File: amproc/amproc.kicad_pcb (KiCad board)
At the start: 2 copper layers, 150 x 70 mm, 130 parts, among them J1 OUT, J2 AC IN, J3 METER BRIDGE, J4 STEREO LINK, J5 LEFT IN, J6 RIGHT IN, J7 CHASSIS, J8 EXT POWER, J9 EXT POWER, Q1 BC556, Q2 BC546, Q3 BC546, Q4 BC556, Q5 BC546, Q6 BC556, Q7 BC556, Q8 BC556, Q9 BC556, U1 TL072, U2 TL072, U3 TL072, U4 LM13700, U5 TL072, U6 TL072, U7 TL072, U8 L7815, U9 L7915

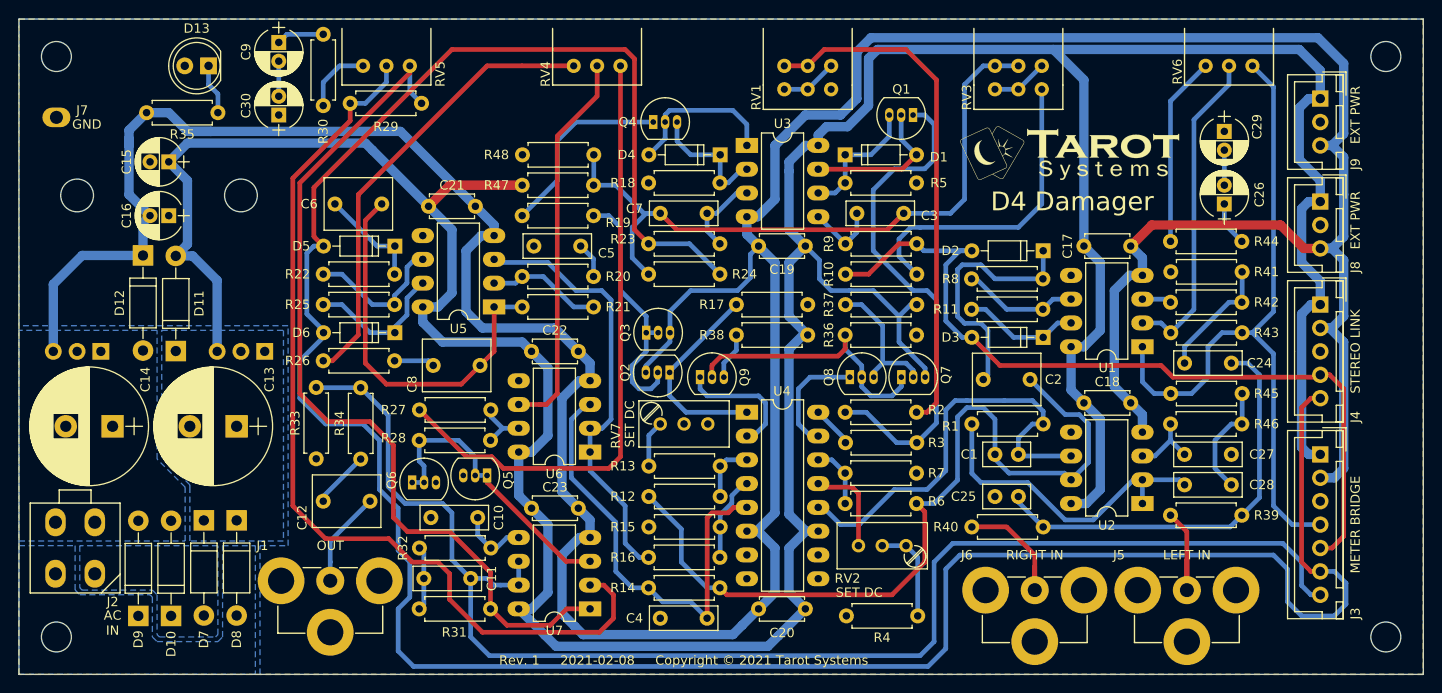
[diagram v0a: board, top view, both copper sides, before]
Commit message: Upgrade amproc to Kicad 6
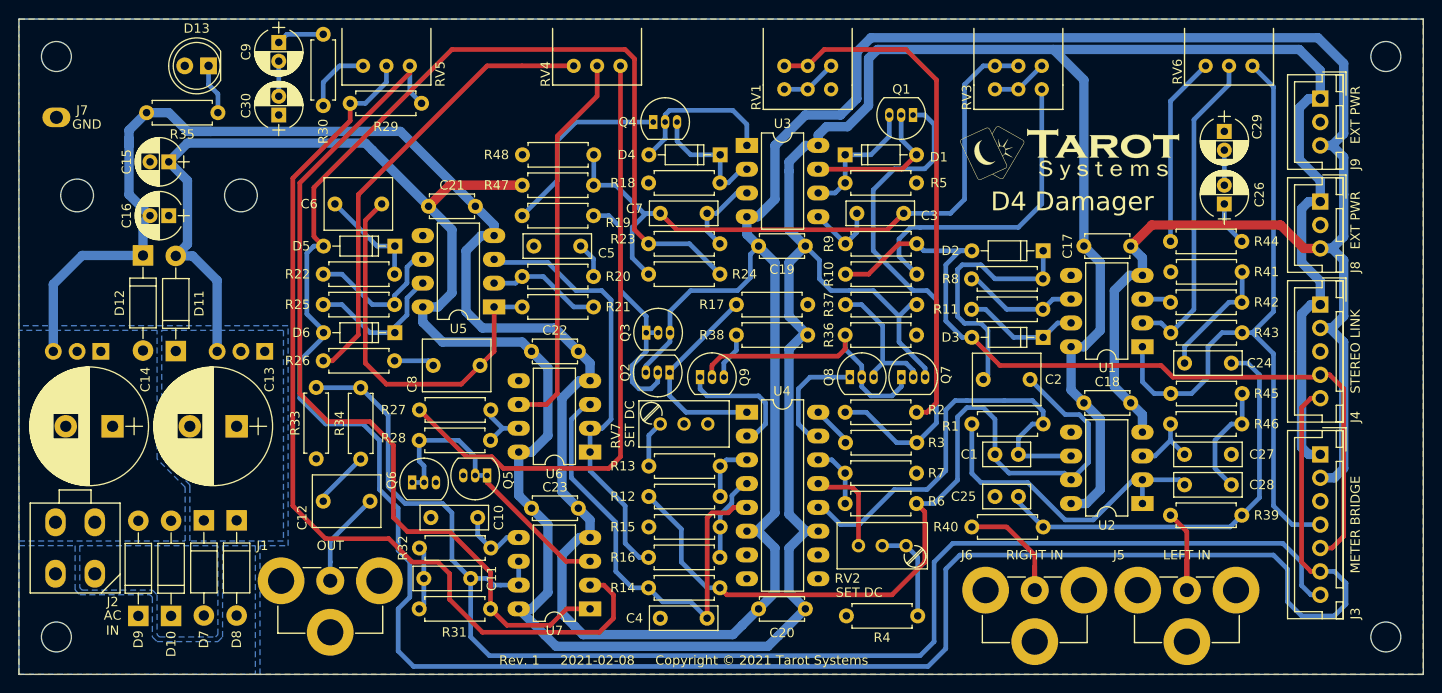
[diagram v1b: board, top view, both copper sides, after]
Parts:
- C25: value 560p -> 100p
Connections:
- net /Limiter.sch/IN renamed /Input stage/OUT
- net /Preemphasis/IN renamed /Limiter.sch/OUT
- U4 pad 10: Net-(U4-Pad10) -> unconnected-(U4-Pad10)
- U4 pad 7: Net-(U4-Pad7) -> unconnected-(U4-Pad7)
- U4 pad 8: Net-(U4-Pad8) -> unconnected-(U4-Pad8)
- U4 pad 9: Net-(U4-Pad9) -> unconnected-(U4-Pad9)
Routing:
- net Net-(C27-Pad2): track 8.39 -> 7.56 mm
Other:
- net class Default removed
- net class Power removed

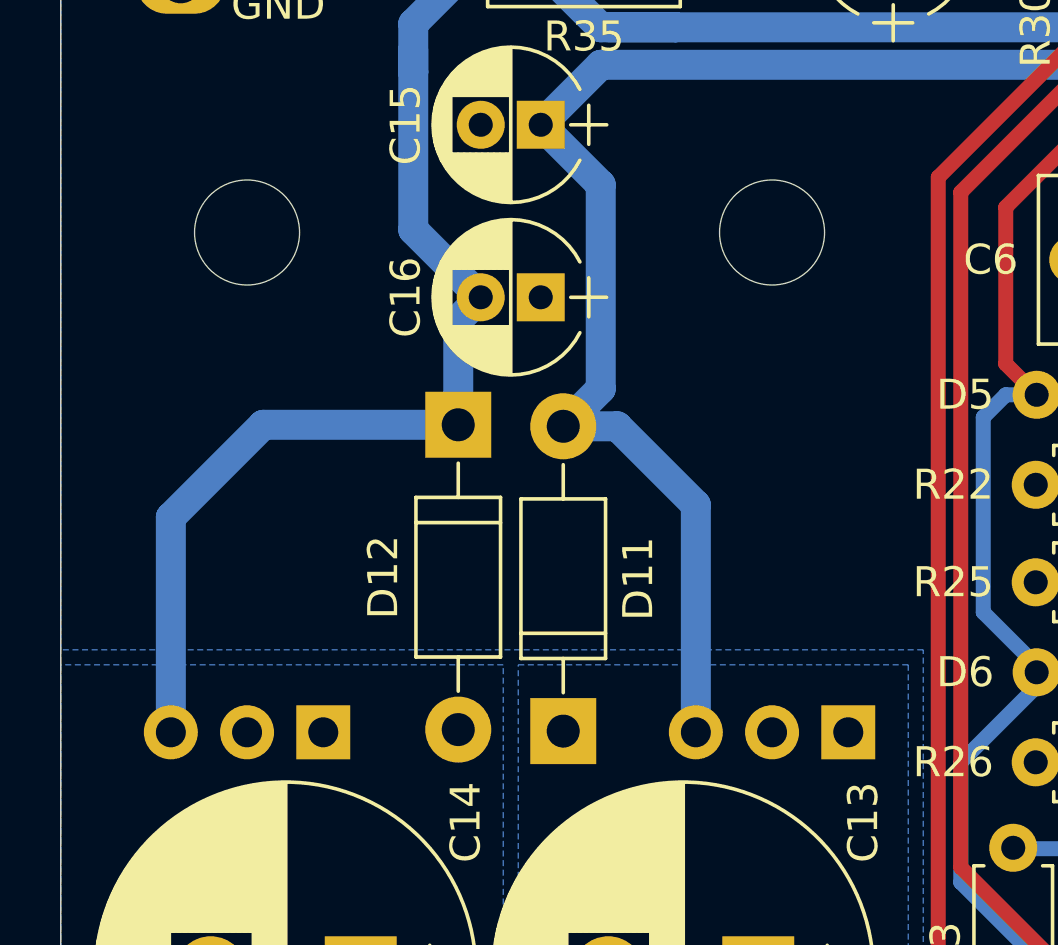
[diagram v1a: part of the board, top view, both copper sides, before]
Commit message: Fix U8, U9 pinouts
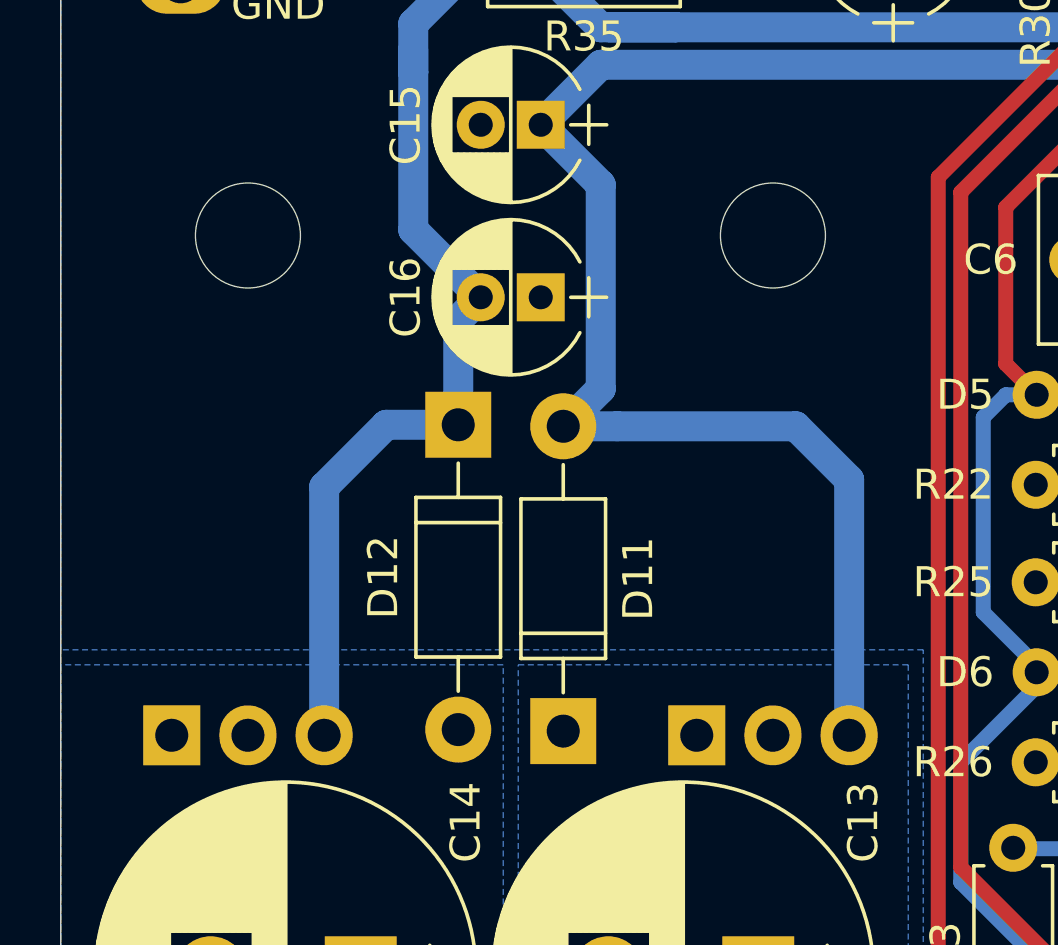
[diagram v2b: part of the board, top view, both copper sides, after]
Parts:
- U8, U9: footprint TO_SOT_Packages_THT:TO-220-3_Horizontal -> Package_TO_SOT_THT:TO-220-3_Horizontal_TabUp
- moved U8 5.05 mm to (91.2, 95.6), turned to 0 degrees
- moved U9 5.05 mm to (73.7, 95.6), turned to 0 degrees
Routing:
- net +15V: track 413.0 -> 418.7 mm
- net -15V: track 411.3 -> 406.9 mm
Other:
- board text added: "1"
- board text added: "3"
